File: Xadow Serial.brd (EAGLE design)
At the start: 28.1 x 20.3 mm, 28 parts, among them J1 CONNECTOR-HEADER-8P-3461050P1, J2 12p 0.5mm bottom contact, J3 12p 0.5mm bottom contact, J4 12p 0.5mm bottom contact, U1 SC16IS750, U2 BSS138PS, X1 CTS_32X25_SMD

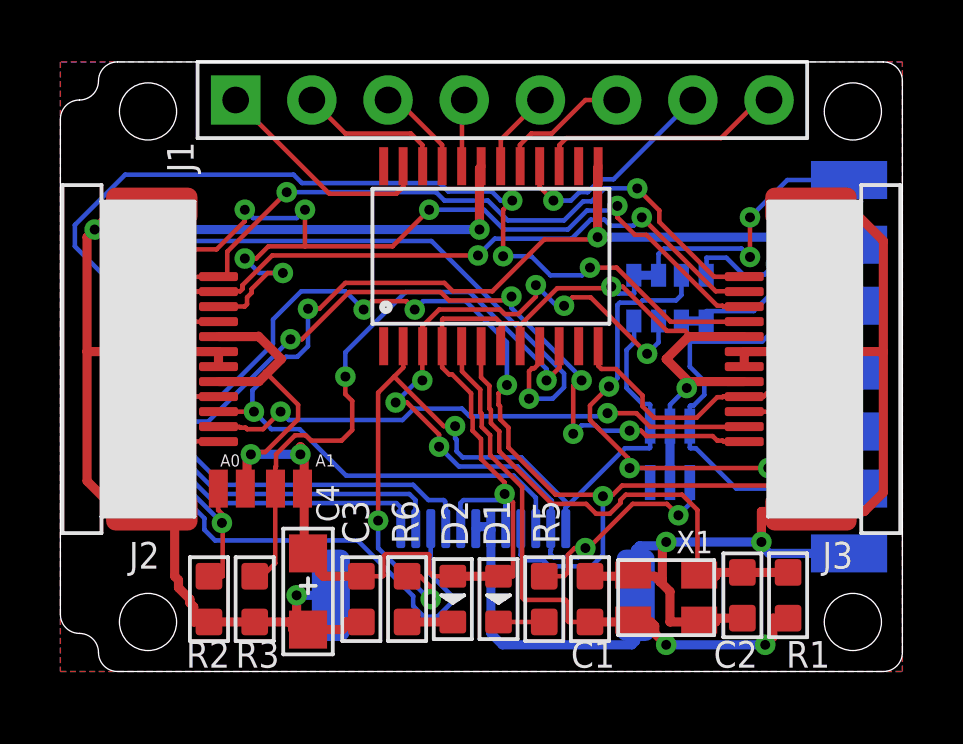
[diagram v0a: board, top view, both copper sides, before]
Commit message: Moved solder jumpers to the bottom
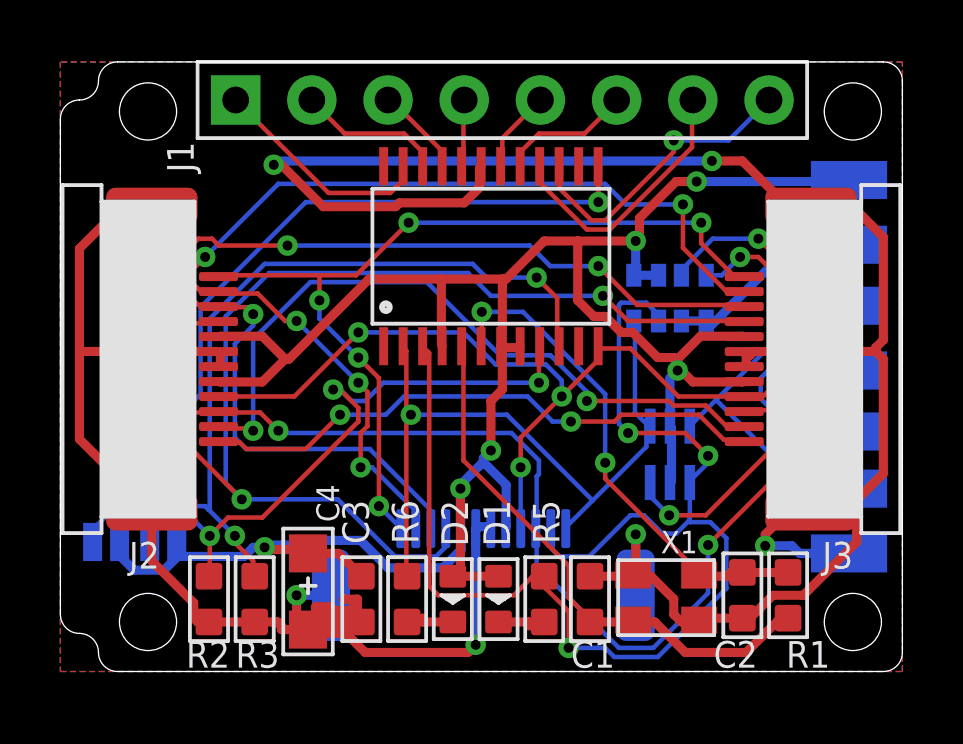
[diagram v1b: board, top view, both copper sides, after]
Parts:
- moved A1 6.35 mm to (1.65, 4.45), flipped to the bottom, turned to 0 degrees
- moved A0 2.90 mm to (3.56, 4.45), flipped to the bottom, turned to 0 degrees
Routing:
- net GND: track 93.1 -> 115.5 mm, vias 5 -> 6
- net PD0/SCL/D3: track 49.0 -> 30.1 mm, vias 6 -> 4
- net PB3/D14/MISO: track 54.2 -> 36.3 mm, vias 7 -> 3
- net N$4: track 32.7 -> 20.8 mm, vias 2 -> 3
- net 3V3: track 69.7 -> 81.3 mm, vias 7 -> 6
- net RX: track 31.0 -> 42.5 mm, vias 8 -> 3
- net PD1/SDA/D2: track 45.8 -> 56.9 mm, vias 6 -> 5
- net PB1/D15/SCK: track 38.6 -> 29.0 mm, vias 3 -> 5
- net N$3: track 20.6 -> 28.4 mm
- net PD3/TXO/D1: track 26.3 -> 19.2 mm, vias 6 -> 2
- net PF0/A5: track 48.3 -> 41.5 mm, vias 5 -> 4
- net PD2/RXI/D0: track 18.4 -> 23.6 mm
- net TX: track 28.1 -> 23.5 mm, vias 3 -> 1
- net RX_5: track 18.7 -> 14.8 mm
- net IO0: track 8.32 -> 10.1 mm, vias 0 -> 1
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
